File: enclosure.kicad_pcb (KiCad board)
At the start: 2 copper layers, 100 x 220 mm, 184 parts, among them J101 Conn_01x06_Socket, J102 Conn_01x02_Socket, J103 Conn_01x02_Socket, J104 Conn_01x02_Socket, J105 Conn_01x02_Socket, Q1001 DPLS350E, U1001 MC7805, U1002 MC7812, U101 4041, U201 Si8641BD-B-IS2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

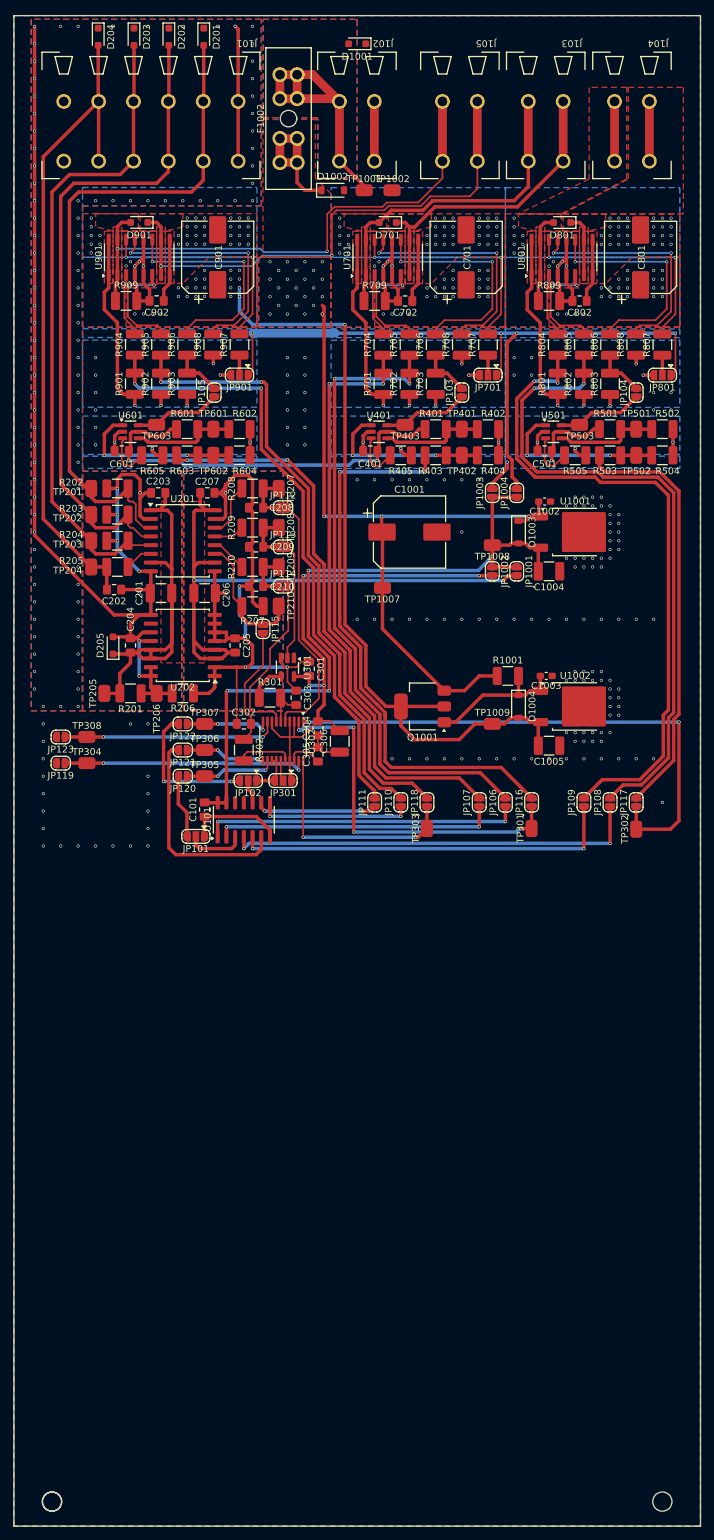
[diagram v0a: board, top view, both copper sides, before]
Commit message: adapt pcb size to 100x125 mm^2
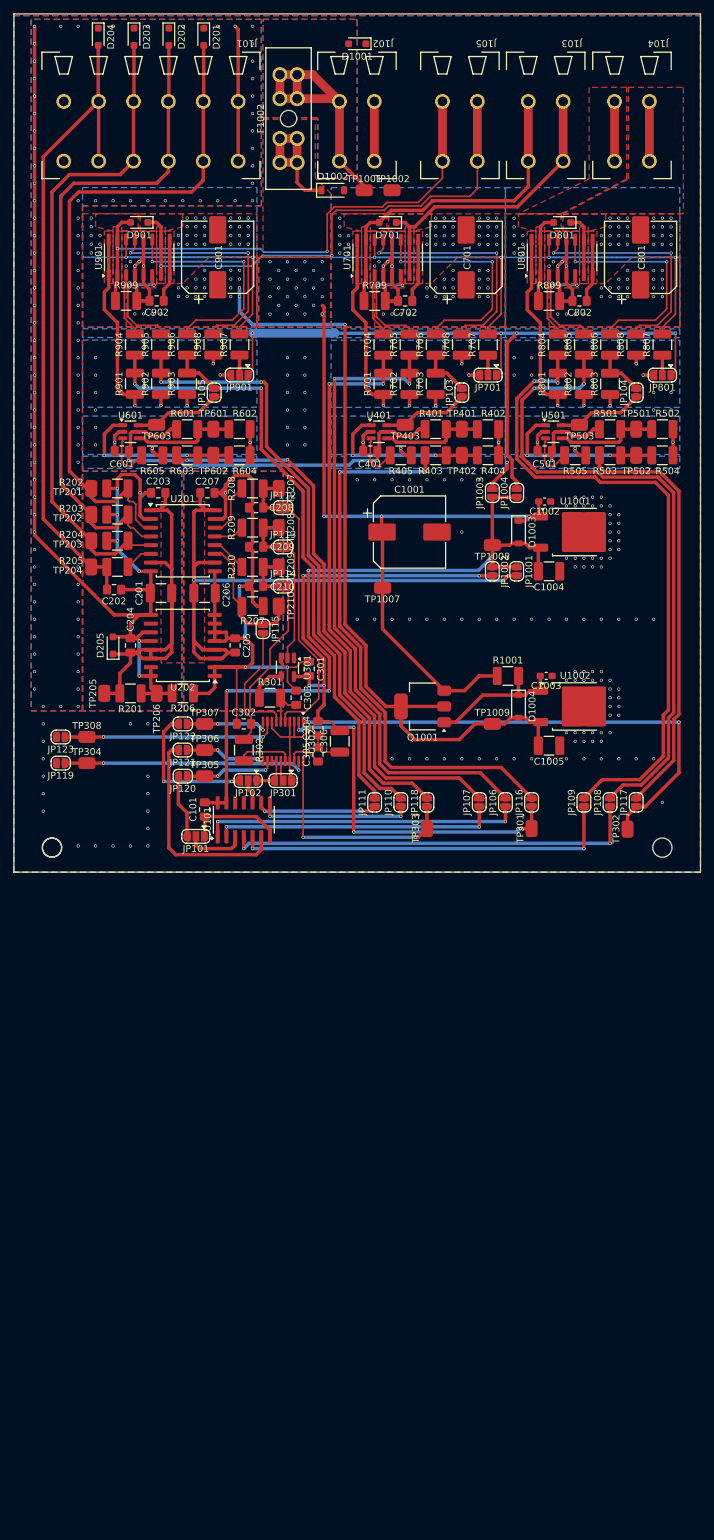
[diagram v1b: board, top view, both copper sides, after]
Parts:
- moved ? 95.2 mm to (155.6, 161.2)
- moved REF** 95.2 mm to (155.6, 161.2)
- moved REF** 95.2 mm to (244.4, 161.2)
- moved TP302 1.27 mm to (239.4, 158.5)
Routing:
- net /dac/dac_ch_1: track 79.1 -> 74.2 mm
- net +5VA_digital-interface: track 90.8 -> 94.6 mm
- net GND: track 295.1 -> 298.4 mm, vias 280 -> 277
- net /fan_-: track 76.2 -> 77.5 mm
- net /fan_+: track 79.5 -> 80.8 mm
- added copper zone on F.Cu, net +5VA_digital-interface
- removed copper zone on B.Cu, net +5VI
- removed copper zone on B.Cu, net /digital-interface/SDI
- removed copper zone on F.Cu, net /digital-interface/SDI
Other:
- board size 100 x 220 mm -> 100 x 125 mm

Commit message: enhance zone edges
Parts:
- moved D201 1.80 mm to (176.4, 44.4), turned to 0 degrees
- moved D202 1.80 mm to (171.3, 44.4), turned to 0 degrees
- moved D203 1.80 mm to (166.2, 44.4), turned to 0 degrees
- moved D204 1.80 mm to (161.0, 44.4), turned to 0 degrees
- moved D1001 0.25 mm to (200.0, 44.4)
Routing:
- net GNDI: vias 105 -> 109

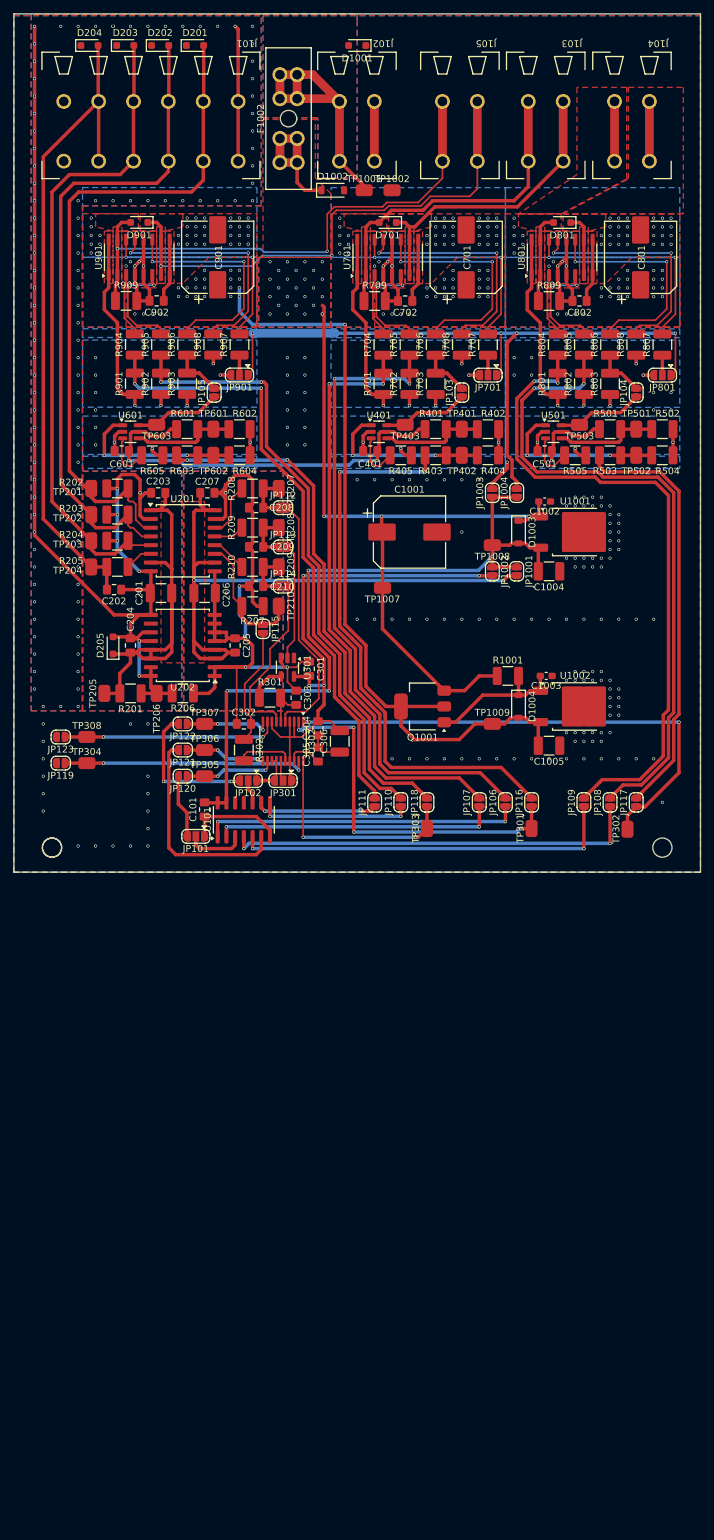
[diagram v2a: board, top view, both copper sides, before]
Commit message: enhance silk screen
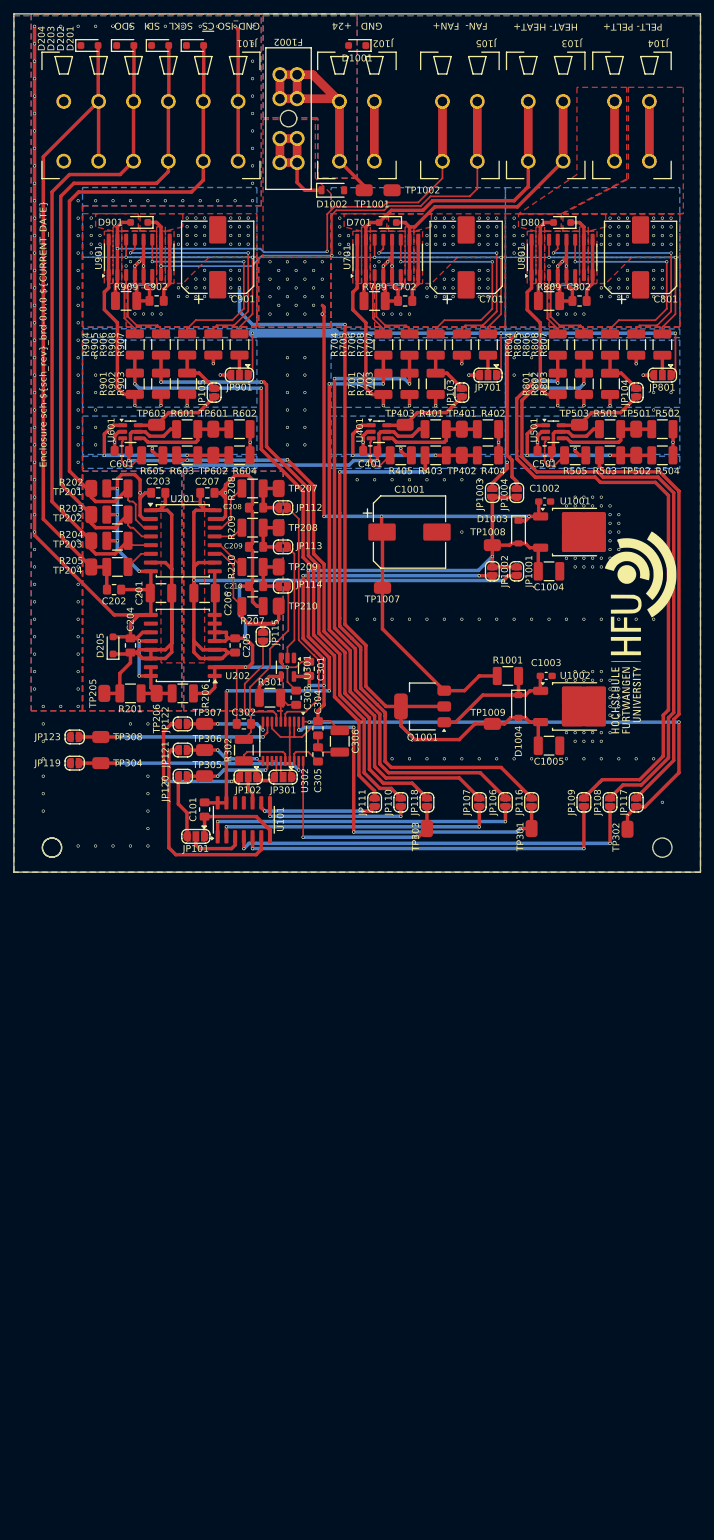
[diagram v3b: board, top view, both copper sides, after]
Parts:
- added G***: LOGO, enclosure:hfu-logo, F.Cu at (241.3, 129.8)
- moved JP119 2.03 mm to (158.9, 148.9)
- moved JP123 2.03 mm to (158.9, 145.1)
- moved TP304 2.03 mm to (162.7, 148.9)
- moved TP308 2.03 mm to (162.7, 145.1)
- moved JP115 1.14 mm to (186.3, 130.5)
- moved JP102 0.51 mm to (184.1, 150.9)
- moved JP301 0.51 mm to (189.2, 150.9)
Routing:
- net /digital-interface/SDO: track 19.4 -> 25.1 mm
- net /dac/dac_ch_7: track 31.3 -> 29.3 mm
- net /dac/dac_ch_3: track 35.8 -> 33.7 mm
- net /SDO: track 17.4 -> 16.2 mm
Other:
- board text added: "${TITLE} sch-${sch_rev}_brd-${REVISION} ${CURRENT_DATE}"
- board text added: "FAN- FAN+"
- board text added: "GND +24"
- board text added: "GND_ISO ~{CS} SCKL SDI SDO"
- board text added: "HEAT- HEAT+"
- board text added: "PELT- PELT+"

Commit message: fix drc errors
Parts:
- removed ?: , 
- REF** (x2): footprint pss:MountingHole_2.8mm -> enclosure:MountingHole_2.8mm
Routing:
- net unconnected-(J101-Pin_6-Pad6): track 0.00 -> 8.70 mm
- net /digital-interface/SDO_ISO: track 96.5 -> 103.6 mm
- net GNDI: vias 109 -> 108
